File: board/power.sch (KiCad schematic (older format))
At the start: 29 parts, among them U201 ADP3303-3V3, U202 ADP3334, U203 ADP3334, U204 LP2985

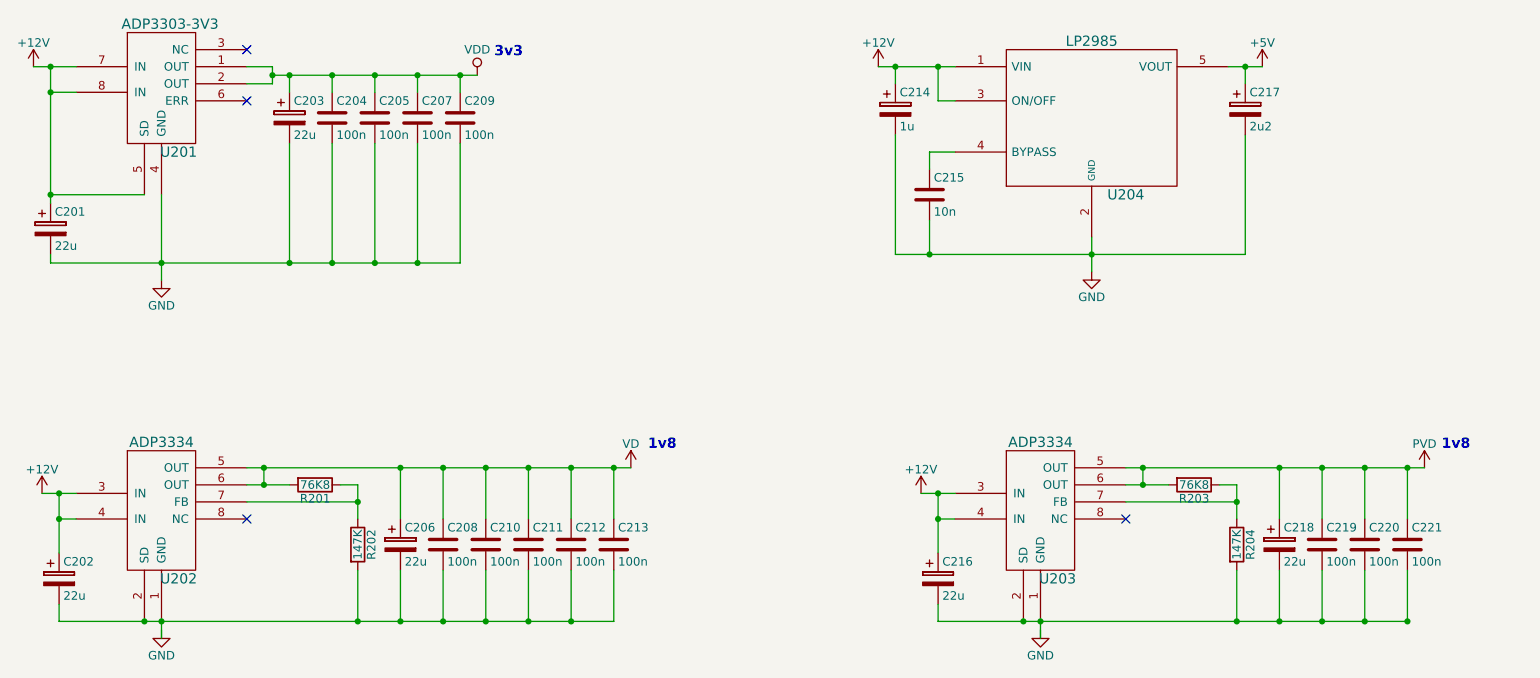
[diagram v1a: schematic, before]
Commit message: Add LEDs to power lines and remove 3v3 regulator
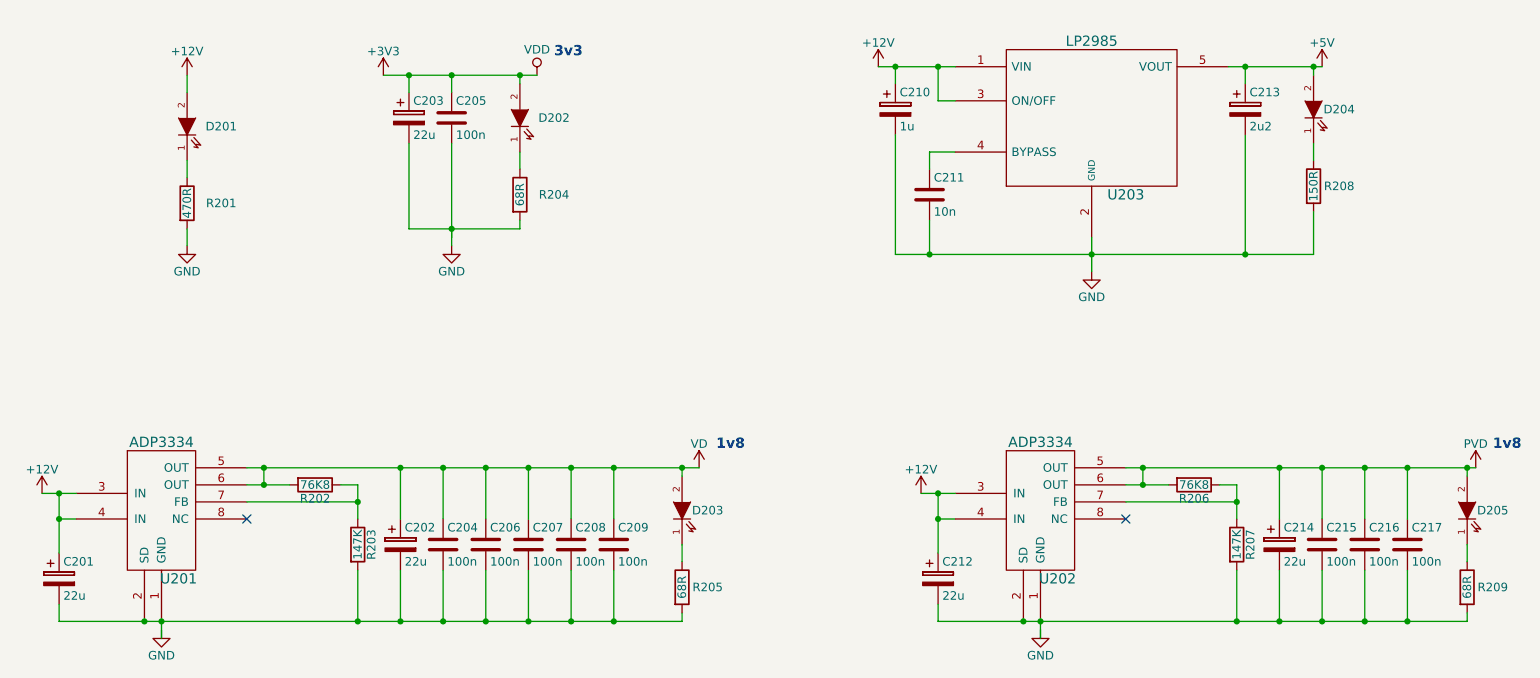
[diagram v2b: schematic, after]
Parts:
- removed C201: 22u, symbol CP
- removed C205, C207, C209: 100n, symbol C
- removed U201: ADP3303-3V3, ~, symbol ADP3303-3v3
- added D201, D202, D203, D204, D205: LED, symbol LED
- added R201: 470R, symbol R
- added R204, R205, R209: 68R, symbol R
- added R208: 150R, symbol R
- renumbered C202 to C201, C206 to C202, C208 to C204, C204 to C205, C210 to C206, C211 to C207, C212 to C208, C213 to C209, C214 to C210, C215 to C211, C216 to C212, C217 to C213, C218 to C214, C219 to C215, C220 to C216, C221 to C217, R201 to R202, R202 to R203, R203 to R206, R204 to R207, U202 to U201, U203 to U202, U204 to U203
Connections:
- net +12V: now also D201.2 (A)
- net +5V: now also D204.2 (A)
- net GND: now also R201.2, R204.2, R208.2
- net PVD: now also D205.2 (A)
- net VD: now also D203.2 (A)
- net at C201.2, C202.2, C204.2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: now also R205.2
- net at C212.2, C214.2, C215.2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: now also R209.2
- net VDD renamed +3V3
- net +3V3: now also D202.2 (A)
- new net: D202.1 (K), R204.1
- new net: D201.1 (K), R201.1
- new net: D204.1 (K), R208.1
- new net: D203.1 (K), R205.1
- new net: D205.1 (K), R209.1
- no-connect marks 4 -> 2
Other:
- moved on the sheet: C203, C205

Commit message: Use the same filtering as before for the 3v3
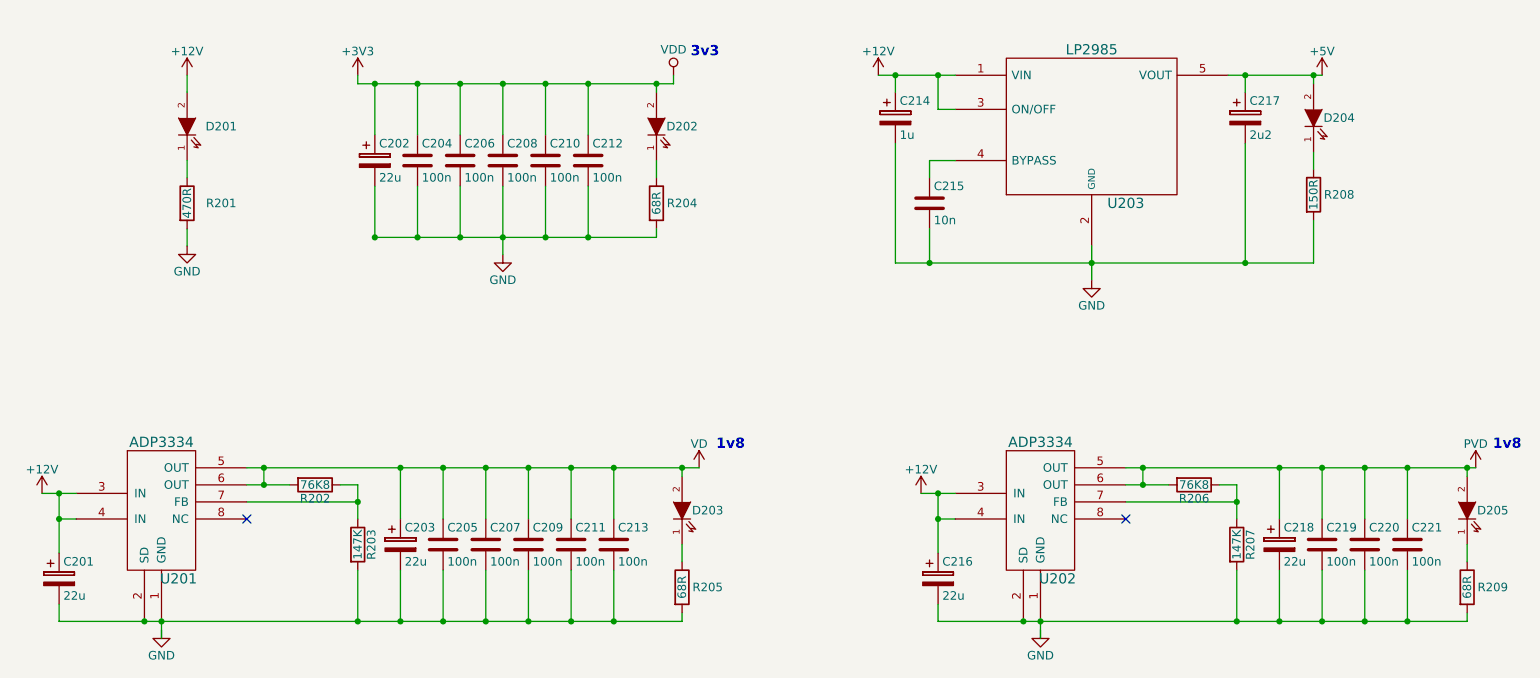
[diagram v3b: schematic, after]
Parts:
- removed C203: 22u, symbol CP
- removed C205: 100n, symbol C
- added C202: 22u, symbol CP
- added C204, C206, C208, C210, C212: 100n, symbol C
- renumbered C202 to C203, C204 to C205, C206 to C207, C207 to C209, C208 to C211, C209 to C213, C210 to C214, C211 to C215, C212 to C216, C213 to C217, C214 to C218, C215 to C219, C216 to C220, C217 to C221
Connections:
- net +3V3: now also C202.1, C204.1, C206.1, C208.1, C210.1, C212.1
- net GND: now also C202.2, C204.2, C206.2, C208.2, C210.2, C212.2
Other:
- moved on the sheet: C214, C215, C217, D204, R208, U203

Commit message: Add correct value for 1v8 power LEDs
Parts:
- R205, R209: value 68R -> 1R
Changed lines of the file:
@@
 Sheet 2 6
 Title "TOFE VGA Expansion Board - Power"
-Date "2016-01-10"
+Date "2016-01-12"
 Rev ""
 Comp "Kenny Duffus <kenny@duffus.org>"
@@
 P 5350 5000
 F 0 "R205" H 5500 5000 50  0000 C CNN
-F 1 "68R" V 5350 5000 50  0000 C CNN
+F 1 "1R" V 5350 5000 50  0000 C CNN
 F 2 "" V 5280 5000 50  0000 C CNN
 F 3 "" H 5350 5000 50  0000 C CNN
@@
 P 9950 5000
 F 0 "R209" H 10100 5000 50  0000 C CNN
-F 1 "68R" V 9950 5000 50  0000 C CNN
+F 1 "1R" V 9950 5000 50  0000 C CNN
 F 2 "" V 9880 5000 50  0000 C CNN
 F 3 "" H 9950 5000 50  0000 C CNN

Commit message: Start assigning footprints
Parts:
- C204, C205, C206, C207, C208, C209, C210, C211, C212, C213, C215, C219, C220, C221, D201, D202, D203, D204, D205, R201, R202, R203, R204, R205, R206, R207, R208, R209: footprint (none) -> Resistors_SMD:R_0805_HandSoldering
- U201, U202: footprint ~ -> (none)

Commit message: More footprint assigning and generated Netlist
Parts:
- D201, D202, D203, D204, D205: footprint Resistors_SMD:R_0805_HandSoldering -> LEDs:LED_0805
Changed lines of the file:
@@
 F 0 "D201" V 2450 2100 50  0000 C CNN
 F 1 "LED" H 2450 2200 50  0001 C CNN
-F 2 "Resistors_SMD:R_0805_HandSoldering" H 2450 2300 50  0001 C CNN
+F 2 "LEDs:LED_0805" H 2450 2300 50  0001 C CNN
 F 3 "" H 2450 2300 50  0000 C CNN
 	1    2450 2300
@@
 F 0 "D204" V 9050 2100 50  0000 C CNN
 F 1 "LED" H 9050 2150 50  0001 C CNN
-F 2 "Resistors_SMD:R_0805_HandSoldering" H 9050 2250 50  0001 C CNN
+F 2 "LEDs:LED_0805" H 9050 2250 50  0001 C CNN
 F 3 "" H 9050 2250 50  0000 C CNN
 	1    9050 2250
@@
 F 0 "D203" V 5350 4400 50  0000 C CNN
 F 1 "LED" H 5350 4450 50  0001 C CNN
-F 2 "Resistors_SMD:R_0805_HandSoldering" H 5350 4550 50  0001 C CNN
+F 2 "LEDs:LED_0805" H 5350 4550 50  0001 C CNN
 F 3 "" H 5350 4550 50  0000 C CNN
 	1    5350 4550
@@
 F 0 "D205" V 9950 4400 50  0000 C CNN
 F 1 "LED" H 9950 4450 50  0001 C CNN
-F 2 "Resistors_SMD:R_0805_HandSoldering" H 9950 4550 50  0001 C CNN
+F 2 "LEDs:LED_0805" H 9950 4550 50  0001 C CNN
 F 3 "" H 9950 4550 50  0000 C CNN
 	1    9950 4550
@@
 F 0 "D202" V 5200 2150 50  0000 C CNN
 F 1 "LED" H 5200 2200 50  0001 C CNN
-F 2 "Resistors_SMD:R_0805_HandSoldering" H 5200 2300 50  0001 C CNN
+F 2 "LEDs:LED_0805" H 5200 2300 50  0001 C CNN
 F 3 "" H 5200 2300 50  0000 C CNN
 	1    5200 2300

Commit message: Found better LED for 1v8
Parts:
- R205, R209: value 1R -> 1R8
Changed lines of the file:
@@
 P 5350 5000
 F 0 "R205" H 5500 5000 50  0000 C CNN
-F 1 "1R" V 5350 5000 50  0000 C CNN
+F 1 "1R8" V 5350 5000 50  0000 C CNN
 F 2 "Resistors_SMD:R_0805_HandSoldering" V 5280 5000 50  0001 C CNN
 F 3 "" H 5350 5000 50  0000 C CNN
@@
 P 9950 5000
 F 0 "R209" H 10100 5000 50  0000 C CNN
-F 1 "1R" V 9950 5000 50  0000 C CNN
+F 1 "1R8" V 9950 5000 50  0000 C CNN
 F 2 "Resistors_SMD:R_0805_HandSoldering" V 9880 5000 50  0001 C CNN
 F 3 "" H 9950 5000 50  0000 C CNN

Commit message: More footprints
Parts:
- C201, C202, C203, C214, C216, C217, C218: footprint (none) -> Capacitors_SMD:c_elec_4x5.8
- U201, U202: footprint (none) -> Housings_SSOP:MSOP-8_3x3mm_Pitch0.65mm
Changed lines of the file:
@@
 LIBS:testpoint
 LIBS:ad9984-power
+LIBS:3-rca
 EELAYER 25 0
 EELAYER END
@@
 F 0 "U201" H 2400 4150 60  0000 C CNN
 F 1 "ADP3334" H 2300 4950 60  0000 C CNN
-F 2 "" H 2100 4650 60  0001 C CNN
+F 2 "Housings_SSOP:MSOP-8_3x3mm_Pitch0.65mm" H 2100 4650 60  0001 C CNN
 F 3 "~" H 2100 4650 60  0000 C CNN
 	1    2300 4550
@@
 F 0 "C203" H 3725 4850 50  0000 L CNN
 F 1 "22u" H 3725 4650 50  0000 L CNN
-F 2 "" H 3738 4600 30  0001 C CNN
+F 2 "Capacitors_SMD:c_elec_4x5.8" H 3738 4600 30  0001 C CNN
 F 3 "" H 3700 4750 60  0000 C CNN
 	1    3700 4750
@@
 F 0 "C201" H 1725 5050 50  0000 L CNN
 F 1 "22u" H 1725 4850 50  0000 L CNN
-F 2 "" H 1738 4800 30  0001 C CNN
+F 2 "Capacitors_SMD:c_elec_4x5.8" H 1738 4800 30  0001 C CNN
 F 3 "" H 1700 4950 60  0000 C CNN
 	1    1700 4950
@@
 F 0 "U202" H 7550 4150 60  0000 C CNN
 F 1 "ADP3334" H 7450 4950 60  0000 C CNN
-F 2 "" H 7250 4650 60  0001 C CNN
+F 2 "Housings_SSOP:MSOP-8_3x3mm_Pitch0.65mm" H 7250 4650 60  0001 C CNN
 F 3 "~" H 7250 4650 60  0000 C CNN
 	1    7450 4550
@@
 F 0 "C218" H 8875 4850 50  0000 L CNN
 F 1 "22u" H 8875 4650 50  0000 L CNN
-F 2 "" H 8888 4600 30  0001 C CNN
+F 2 "Capacitors_SMD:c_elec_4x5.8" H 8888 4600 30  0001 C CNN
 F 3 "" H 8850 4750 60  0000 C CNN
 	1    8850 4750
@@
 F 0 "C216" H 6875 5050 50  0000 L CNN
 F 1 "22u" H 6875 4850 50  0000 L CNN
-F 2 "" H 6888 4800 30  0001 C CNN
+F 2 "Capacitors_SMD:c_elec_4x5.8" H 6888 4800 30  0001 C CNN
 F 3 "" H 6850 4950 60  0000 C CNN
 	1    6850 4950
@@
 F 0 "C217" H 8675 2350 50  0000 L CNN
 F 1 "2u2" H 8675 2150 50  0000 L CNN
-F 2 "" H 8688 2100 30  0001 C CNN
+F 2 "Capacitors_SMD:c_elec_4x5.8" H 8688 2100 30  0001 C CNN
 F 3 "" H 8650 2250 60  0000 C CNN
 	1    8650 2250
@@
 F 0 "C214" H 6625 2350 50  0000 L CNN
 F 1 "1u" H 6625 2150 50  0000 L CNN
-F 2 "" H 6638 2100 30  0001 C CNN
+F 2 "Capacitors_SMD:c_elec_4x5.8" H 6638 2100 30  0001 C CNN
 F 3 "" H 6600 2250 60  0000 C CNN
 	1    6600 2250
@@
 F 0 "C202" H 3575 2600 50  0000 L CNN
 F 1 "22u" H 3575 2400 50  0000 L CNN
-F 2 "" H 3588 2350 30  0001 C CNN
+F 2 "Capacitors_SMD:c_elec_4x5.8" H 3588 2350 30  0001 C CNN
 F 3 "" H 3550 2500 60  0000 C CNN
 	1    3550 2500
